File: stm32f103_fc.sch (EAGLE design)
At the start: 49 parts, among them IC1 STM32F10XCXT6, IC2 LD1117AS33TR, U2 9DoF IMU, Y1 8MHz, Y2 32.768MHz

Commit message: version 2.0
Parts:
- removed C11, C13, C14, C7: 0.1uF, SparkFun-Capacitors:0.1UF-0402-16V-10%
- removed S1: SPST-SMD-5.2, SparkFun-Switches:MOMENTARY-SWITCH-SPST-SMD-5.2-REDUNDANT
- removed U2: 9DoF IMU, SparkFun-Sensors:MPU-9250
- added BUZZER: CMT-1285C-035, SparkFun-Electromechanical:BUZZER-PTH
- added C15, C22: 0.1uF, SparkFun-Capacitors:0.1UF-0402-16V-10%
- added C19: 2.2nF, SparkFun-Capacitors:2.2NF/2200PF-0603-50V-10%
- added C23: 10nF, SparkFun-Capacitors:10NF-0603-50V-10%
- added IMU: MPU-6050, MPU-6050:MPU-6050
- added SWITCH: MOMENTARY-SWITCH-SPST-SMD-4.5MM-轻触开关, SparkFun-Switches:MOMENTARY-SWITCH-SPST-SMD-4.5MM
- C18: device SparkFun-Capacitors:0.1UF-0603-25V-(+80/-20%) -> SparkFun-Capacitors:0.1UF-0402-16V-10%
- C5: value 10nF -> 0.1uF; device SparkFun-Capacitors:10NF-0603-50V-10% -> SparkFun-Capacitors:0.1UF-0402-16V-10%
- C6: device SparkFun-Capacitors:0.1UF-0402-16V-10% -> SparkFun-Capacitors:0.1UF-0603-25V-(+80/-20%)
- HEADER: value (none) -> 2.54mm 2PX3P header
- IC1: value STM32F10XCXT6 -> STM32F103C8T6
- LED1, LED2: value GREEN -> BL-HGE36G-AV-TRB
- MICRO-USB: value (none) -> Micro-USB-5P-无柱-SMD
- N-CHANNEL-MOSFET, N-CHANNEL-MOSFET-2: value (none) -> 2N7002KT1G
- POWER_INPUT: value (none) -> KF350-2P-terminal-block-接线端子
- PY1, PY2: value 1X2-3.5MM -> 1X2-3.5MM KF350 terminal block
- R10, R13: value 22 -> 22omh
- R11, R9: value 680 -> 680omh
- R4, R5: value 470 -> 470omh
- SERVO_X, SERVO_Y: value (none) -> 2.54mm 3P header
- SWD: value (none) -> 2.54mm 4P header
- renumbered D1 to LED1, D2 to LED2, J3 to MICRO-USB, Q1 to N-CHANNEL-MOSFET, Q2 to N-CHANNEL-MOSFET-2
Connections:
- removed net N$11: C6.2, U2.REGOUT
- removed net N$28: IC1POWER.VSS_2
- removed net N$30: IC1POWER.VDD_2
- removed net N$31: IC1POWER.VDD_1
- removed net VBAT: IC1AN_POWER.VBAT
- new net N$16: C22.2, IMU.REGOUT
- new net N$4: C19.1, IMU.CPOUT
- net 9V: now also C6.2; no longer MICRO-USB.VBUS
- net GND: now also BUZZER.2, C15.1, C18.1, C19.2, C22.1, C23.1, C4.2, C5.1, C8.2, IC1POWER.VSS_2, IMU.CLKIN, IMU.FSYNC, IMU.GND, SWITCH.1; no longer C11.2, C13.2, C14.2, C18.2, C5.2, C6.1, C7.2, S1.1, U2.FSYNC, U2.GND
- net N$10: now also C6.1, MICRO-USB.VBUS; no longer C4.2, C8.2
- net PA12: no longer U2.INT
- net PB0: now also IMU.INT
- net PB1: now also BUZZER.1
- net PB8: now also IMU.SDA; no longer U2.SDA/SDI
- net PB9: now also IMU.SCL; no longer U2.SCL/SCLK
- net RESET: now also SWITCH.2; no longer S1.2
- net VCC3V3: now also C15.2, C18.2, C23.2, C5.2, IC1AN_POWER.VBAT, IC1POWER.VDD_1, IC1POWER.VDD_2, IMU.VDD, IMU.VLOGIC; no longer C11.1, C13.1, C14.1, C18.1, C5.1, C7.1, U2.!CS, U2.VDD, U2.VDDIO
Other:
- note removed: "checked"
- moved on the sheet: C18, C5, C6

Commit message: version 1.0.1 done fix transistor
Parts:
- removed N-CHANNEL-MOSFET: 2N7002KT1G, adafruit:MOSFET-NREFLOW
- removed R12: 1omh, SparkFun-Resistors:1OHM-0603-1/10W-1%
- added MOSFET-1: 2N7002KT1G, adafruit:MOSFET-NREFLOW
- added R14: 470omh, SparkFun-Resistors:470OHM-0603-1/10W-1%
- R4: value 470omh -> 1omh; device SparkFun-Resistors:470OHM-0603-1/10W-1% -> SparkFun-Resistors:1OHM-0603-1/10W-1%
- renumbered N-CHANNEL-MOSFET-2 to MOSFET-2
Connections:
- removed net N$15: N-CHANNEL-MOSFET.D, R12.1
- new net N$11: PY1.2, R4.2
- net GND: now also MOSFET-1.D, MOSFET-2.D, R14.2, R5.2; no longer MOSFET-2.S, N-CHANNEL-MOSFET.S, R4.1, R5.1
- net N$13: now also MOSFET-2.S; no longer MOSFET-2.D
- net N$14: now also MOSFET-1.S, R4.1; no longer PY1.2, R12.2
- net PB6: now also R14.1; no longer R5.2
- net PB7: now also MOSFET-1.G, R5.1; no longer N-CHANNEL-MOSFET.G, R4.2
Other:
- moved on the sheet: R15, R4, R5

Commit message: added new switch
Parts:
- SWITCH: device SparkFun-Switches:MOMENTARY-SWITCH-SPST-SMD-4.5MM -> SparkFun-Switches:MOMENTARY-SWITCH-SPST-SMD-6.0X3.5MM
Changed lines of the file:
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@@
 <?xml version="1.0" encoding="utf-8"?>
 <!DOCTYPE eagle SYSTEM "eagle.dtd">
-<eagle version="9.3.1">
+<eagle version="9.3.0">
 <drawing>
 <settings>
@@
 <grid distance="0.1" unitdist="inch" unit="inch" style="lines" multiple="1" display="no" altdistance="0.01" altunitdist="inch" altunit="inch"/>
 <layers>
-<layer number="1" name="Top" color="4" fill="1" visible="no" active="no"/>
-<layer number="16" name="Bottom" color="1" fill="1" visible="no" active="no"/>
-<layer number="17" name="Pads" color="2" fill="1" visible="no" active="no"/>
-<layer number="18" name="Vias" color="2" fill="1" visible="no" active="no"/>
-<layer number="19" name="Unrouted" color="6" fill="1" visible="no" active="no"/>
-<layer number="20" name="Dimension" color="24" fill="1" visible="no" active="no"/>
-<layer number="21" name="tPlace" color="7" fill="1" visible="no" active="no"/>
-<layer number="22" name="bPlace" color="7" fill="1" visible="no" active="no"/>
-<layer number="23" name="tOrigins" color="15" fill="1" visible="no" active="no"/>
-<layer number="24" name="bOrigins" color="15" fill="1" visible="no" active="no"/>
-<layer number="25" name="tNames" color="7" fill="1" visible="no" active="no"/>
-<layer number="26" name="bNames" color="7" fill="1" visible="no" active="no"/>
-<layer number="27" name="tValues" color="7" fill="1" visible="no" active="no"/>
-<layer number="28" name="bValues" color="7" fill="1" visible="no" active="no"/>
+<layer number="1" name="Top" color="4" fill="1" visible="yes" active="no"/>
+<layer number="16" name="Bottom" color="1" fill="1" visible="yes" active="no"/>
+<layer number="17" name="Pads" color="2" fill="1" visible="yes" active="no"/>
+<layer number="18" name="Vias" color="2" fill="1" visible="yes" active="no"/>
+<layer number="19" name="Unrouted" color="6" fill="1" visible="yes" active="no"/>
+<layer number="20" name="Dimension" color="24" fill="1" visible="yes" active="no"/>
+<layer number="21" name="tPlace" color="7" fill="1" visible="yes" active="no"/>
+<layer number="22" name="bPlace" color="7" fill="1" visible="yes" active="no"/>
+<layer number="23" name="tOrigins" color="15" fill="1" visible="yes" active="no"/>
+<layer number="24" name="bOrigins" color="15" fill="1" visible="yes" active="no"/>
+<layer number="25" name="tNames" color="7" fill="1" visible="yes" active="no"/>
+<layer number="26" name="bNames" color="7" fill="1" visible="yes" active="no"/>
+<layer number="27" name="tValues" color="7" fill="1" visible="yes" active="no"/>
+<layer number="28" name="bValues" color="7" fill="1" visible="yes" active="no"/>
 <layer number="29" name="tStop" color="7" fill="3" visible="no" active="no"/>
 <layer number="30" name="bStop" color="7" fill="6" visible="no" active="no"/>
@@
 <layer number="35" name="tGlue" color="7" fill="4" visible="no" active="no"/>
 <layer number="36" name="bGlue" color="7" fill="5" visible="no" active="no"/>
-<layer number="37" name="tTest" color="7" fill="1" visible="no" active="no"/>
-<layer number="38" name="bTest" color="7" fill="1" visible="no" active="no"/>
+<layer number="37" name="tTest" color="7" fill="1" visible="yes" active="no"/>
+<layer number="38" name="bTest" color="7" fill="1" visible="yes" active="no"/>
 <layer number="39" name="tKeepout" color="4" fill="11" visible="no" active="no"/>
 <layer number="40" name="bKeepout" color="1" fill="11" visible="no" active="no"/>
@@
 <layer number="44" name="Drills" color="7" fill="1" visible="no" active="no"/>
 <layer number="45" name="Holes" color="7" fill="1" visible="no" active="no"/>
-<layer number="46" name="Milling" color="3" fill="1" visible="no" active="no"/>
-<layer number="47" name="Measures" color="7" fill="1" visible="no" active="no"/>
-<layer number="48" name="Document" color="7" fill="1" visible="no" active="no"/>
-<layer number="49" name="Reference" color="7" fill="1" visible="no" active="no"/>
-<layer number="50" name="dxf" color="7" fill="1" visible="no" active="no"/>
-<layer number="51" name="tDocu" color="7" fill="1" visible="no" active="no"/>
-<layer number="52" name="bDocu" color="7" fill="1" visible="no" active="no"/>
-<layer number="53" name="tGND_GNDA" color="7" fill="9" visible="no" active="no"/>
-<layer number="54" name="bGND_GNDA" color="1" fill="9" visible="no" active="no"/>
-<layer number="56" name="wert" color="7" fill="1" visible="no" active="no"/>
-<layer number="57" name="tCAD" color="7" fill="1" visible="no" active="no"/>
-<layer number="59" name="tCarbon" color="7" fill="1" visible="no" active="no"/>
-<layer number="60" name="bCarbon" color="7" fill="1" visible="no" active="no"/>
+<layer number="46" name="Milling" color="3" fill="1" visible="yes" active="no"/>
+<layer number="47" name="Measures" color="7" fill="1" visible="yes" active="no"/>
+<layer number="48" name="Document" color="7" fill="1" visible="yes" active="no"/>
+<layer number="49" name="Reference" color="7" fill="1" visible="yes" active="no"/>
+<layer number="50" name="dxf" color="7" fill="1" visible="yes" active="no"/>
+<layer number="51" name="tDocu" color="7" fill="1" visible="yes" active="no"/>
+<layer number="52" name="bDocu" color="7" fill="1" visible="yes" active="no"/>
+<layer number="53" name="tGND_GNDA" color="7" fill="9" visible="yes" active="no"/>
+<layer number="54" name="bGND_GNDA" color="1" fill="9" visible="yes" active="no"/>
+<layer number="56" name="wert" color="7" fill="1" visible="yes" active="no"/>
+<layer number="57" name="tCAD" color="7" fill="1" visible="yes" active="no"/>
+<layer number="59" name="tCarbon" color="7" fill="1" visible="yes" active="no"/>
+<layer number="60" name="bCarbon" color="7" fill="1" visible="yes" active="no"/>
 <layer number="88" name="SimResults" color="9" fill="1" visible="yes" active="yes"/>
 <layer number="89" name="SimProbes" color="9" fill="1" visible="yes" active="yes"/>
@@
 <part name="C18" library="SparkFun-Capacitors" deviceset="0.1UF" device="-0402-16V-10%" value="0.1uF"/>
 <part name="GND12" library="SparkFun-PowerSymbols" library_urn="urn:adsk.eagle:library:530" deviceset="GND" device=""/>
-<part name="SWITCH" library="SparkFun-Switches" library_urn="urn:adsk.eagle:library:535" deviceset="MOMENTARY-SWITCH-SPST" device="-SMD-4.5MM" package3d_urn="urn:adsk.eagle:package:40162/1" value="MOMENTARY-SWITCH-SPST-SMD-4.5MM-轻触开关"/>
+<part name="SWITCH" library="SparkFun-Switches" library_urn="urn:adsk.eagle:library:535" deviceset="MOMENTARY-SWITCH-SPST" device="-SMD-6.0X3.5MM" package3d_urn="urn:adsk.eagle:package:40165/1" value="MOMENTARY-SWITCH-SPST-SMD-4.5MM-轻触开关"/>
 <part name="R14" library="SparkFun-Resistors" library_urn="urn:adsk.eagle:library:532" deviceset="470OHM" device="-0603-1/10W-1%" package3d_urn="urn:adsk.eagle:package:39650/1" value="470omh"/>
 <part name="GND13" library="SparkFun-PowerSymbols" library_urn="urn:adsk.eagle:library:530" deviceset="GND" device=""/>

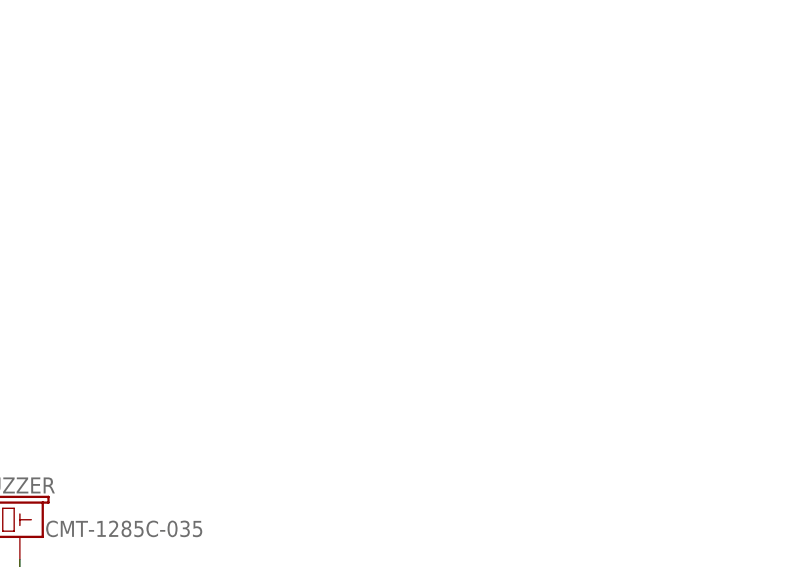
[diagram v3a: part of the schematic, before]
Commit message: added serial port
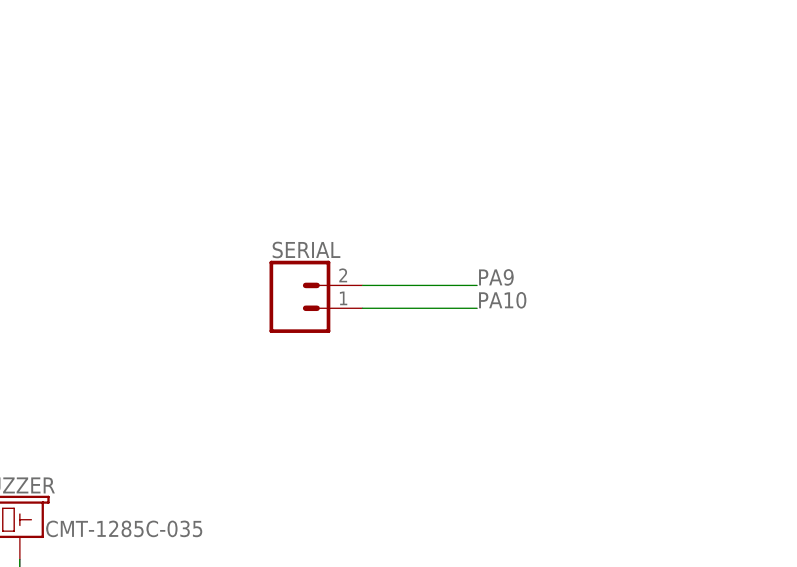
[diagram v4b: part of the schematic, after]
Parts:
- added SERIAL: (no value), SparkFun-Connectors:CONN_02
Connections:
- net PA10: now also SERIAL.1
- net PA9: now also SERIAL.2
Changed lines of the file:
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@@
 <grid distance="0.1" unitdist="inch" unit="inch" style="lines" multiple="1" display="no" altdistance="0.01" altunitdist="inch" altunit="inch"/>
 <layers>
-<layer number="1" name="Top" color="4" fill="1" visible="yes" active="no"/>
-<layer number="16" name="Bottom" color="1" fill="1" visible="yes" active="no"/>
-<layer number="17" name="Pads" color="2" fill="1" visible="yes" active="no"/>
-<layer number="18" name="Vias" color="2" fill="1" visible="yes" active="no"/>
-<layer number="19" name="Unrouted" color="6" fill="1" visible="yes" active="no"/>
-<layer number="20" name="Dimension" color="24" fill="1" visible="yes" active="no"/>
-<layer number="21" name="tPlace" color="7" fill="1" visible="yes" active="no"/>
-<layer number="22" name="bPlace" color="7" fill="1" visible="yes" active="no"/>
-<layer number="23" name="tOrigins" color="15" fill="1" visible="yes" active="no"/>
-<layer number="24" name="bOrigins" color="15" fill="1" visible="yes" active="no"/>
-<layer number="25" name="tNames" color="7" fill="1" visible="yes" active="no"/>
-<layer number="26" name="bNames" color="7" fill="1" visible="yes" active="no"/>
-<layer number="27" name="tValues" color="7" fill="1" visible="yes" active="no"/>
-<layer number="28" name="bValues" color="7" fill="1" visible="yes" active="no"/>
+<layer number="1" name="Top" color="4" fill="1" visible="no" active="no"/>
+<layer number="2" name="Route2" color="16" fill="1" visible="no" active="no"/>
+<layer number="3" name="Route3" color="17" fill="1" visible="no" active="no"/>
+<layer number="4" name="Route4" color="18" fill="1" visible="no" active="no"/>
+<layer number="5" name="Route5" color="19" fill="1" visible="no" active="no"/>
+<layer number="6" name="Route6" color="25" fill="1" visible="no" active="no"/>
+<layer number="7" name="Route7" color="26" fill="1" visible="no" active="no"/>
+<layer number="8" name="Route8" color="27" fill="1" visible="no" active="no"/>
+<layer number="9" name="Route9" color="28" fill="1" visible="no" active="no"/>
+<layer number="10" name="Route10" color="29" fill="1" visible="no" active="no"/>
+<layer number="11" name="Route11" color="30" fill="1" visible="no" active="no"/>
+<layer number="12" name="Route12" color="20" fill="1" visible="no" active="no"/>
+<layer number="13" name="Route13" color="21" fill="1" visible="no" active="no"/>
+<layer number="14" name="Route14" color="22" fill="1" visible="no" active="no"/>
+<layer number="15" name="Route15" color="23" fill="1" visible="no" active="no"/>
+<layer number="16" name="Bottom" color="1" fill="1" visible="no" active="no"/>
+<layer number="17" name="Pads" color="2" fill="1" visible="no" active="no"/>
+<layer number="18" name="Vias" color="2" fill="1" visible="no" active="no"/>
+<layer number="19" name="Unrouted" color="6" fill="1" visible="no" active="no"/>
+<layer number="20" name="Dimension" color="24" fill="1" visible="no" active="no"/>
+<layer number="21" name="tPlace" color="7" fill="1" visible="no" active="no"/>
+<layer number="22" name="bPlace" color="7" fill="1" visible="no" active="no"/>
+<layer number="23" name="tOrigins" color="15" fill="1" visible="no" active="no"/>
+<layer number="24" name="bOrigins" color="15" fill="1" visible="no" active="no"/>
+<layer number="25" name="tNames" color="7" fill="1" visible="no" active="no"/>
+<layer number="26" name="bNames" color="7" fill="1" visible="no" active="no"/>
+<layer number="27" name="tValues" color="7" fill="1" visible="no" active="no"/>
+<layer number="28" name="bValues" color="7" fill="1" visible="no" active="no"/>
 <layer number="29" name="tStop" color="7" fill="3" visible="no" active="no"/>
 <layer number="30" name="bStop" color="7" fill="6" visible="no" active="no"/>
@@
 <layer number="35" name="tGlue" color="7" fill="4" visible="no" active="no"/>
 <layer number="36" name="bGlue" color="7" fill="5" visible="no" active="no"/>
-<layer number="37" name="tTest" color="7" fill="1" visible="yes" active="no"/>
-<layer number="38" name="bTest" color="7" fill="1" visible="yes" active="no"/>
+<layer number="37" name="tTest" color="7" fill="1" visible="no" active="no"/>
+<layer number="38" name="bTest" color="7" fill="1" visible="no" active="no"/>
 <layer number="39" name="tKeepout" color="4" fill="11" visible="no" active="no"/>
 <layer number="40" name="bKeepout" color="1" fill="11" visible="no" active="no"/>
@@
 <layer number="44" name="Drills" color="7" fill="1" visible="no" active="no"/>
 <layer number="45" name="Holes" color="7" fill="1" visible="no" active="no"/>
-<layer number="46" name="Milling" color="3" fill="1" visible="yes" active="no"/>
-<layer number="47" name="Measures" color="7" fill="1" visible="yes" active="no"/>
-<layer number="48" name="Document" color="7" fill="1" visible="yes" active="no"/>
-<layer number="49" name="Reference" color="7" fill="1" visible="yes" active="no"/>
-<layer number="50" name="dxf" color="7" fill="1" visible="yes" active="no"/>
-<layer number="51" name="tDocu" color="7" fill="1" visible="yes" active="no"/>
-<layer number="52" name="bDocu" color="7" fill="1" visible="yes" active="no"/>
-<layer number="53" name="tGND_GNDA" color="7" fill="9" visible="yes" active="no"/>
-<layer number="54" name="bGND_GNDA" color="1" fill="9" visible="yes" active="no"/>
-<layer number="56" name="wert" color="7" fill="1" visible="yes" active="no"/>
-<layer number="57" name="tCAD" color="7" fill="1" visible="yes" active="no"/>
-<layer number="59" name="tCarbon" color="7" fill="1" visible="yes" active="no"/>
-<layer number="60" name="bCarbon" color="7" fill="1" visible="yes" active="no"/>
+<layer number="46" name="Milling" color="3" fill="1" visible="no" active="no"/>
+<layer number="47" name="Measures" color="7" fill="1" visible="no" active="no"/>
+<layer number="48" name="Document" color="7" fill="1" visible="no" active="no"/>
+<layer number="49" name="Reference" color="7" fill="1" visible="no" active="no"/>
+<layer number="50" name="dxf" color="7" fill="1" visible="no" active="no"/>
+<layer number="51" name="tDocu" color="7" fill="1" visible="no" active="no"/>
+<layer number="52" name="bDocu" color="7" fill="1" visible="no" active="no"/>
+<layer number="53" name="tGND_GNDA" color="7" fill="9" visible="no" active="no"/>
+<layer number="54" name="bGND_GNDA" color="1" fill="9" visible="no" active="no"/>
+<layer number="56" name="wert" color="7" fill="1" visible="no" active="no"/>
+<layer number="57" name="tCAD" color="7" fill="1" visible="no" active="no"/>
+<layer number="59" name="tCarbon" color="7" fill="1" visible="no" active="no"/>
+<layer number="60" name="bCarbon" color="7" fill="1" visible="no" active="no"/>
 <layer number="88" name="SimResults" color="9" fill="1" visible="yes" active="yes"/>
 <layer number="89" name="SimProbes" color="9" fill="1" visible="yes" active="yes"/>
@@
 <part name="R5" library="SparkFun-Resistors" library_urn="urn:adsk.eagle:library:532" deviceset="470OHM" device="-0603-1/10W-1%" package3d_urn="urn:adsk.eagle:package:39650/1" value="470omh"/>
 <part name="GND14" library="SparkFun-PowerSymbols" library_urn="urn:adsk.eagle:library:530" deviceset="GND" device=""/>
+<part name="SERIAL" library="SparkFun-Connectors" library_urn="urn:adsk.eagle:library:513" deviceset="CONN_02" device="" package3d_urn="urn:adsk.eagle:package:38039/1"/>
 </parts>
 <sheets>
@@
 <instance part="GND14" gate="1" x="-50.8" y="200.66" smashed="yes" rot="R180">
 <attribute name="VALUE" x="-50.8" y="200.914" size="1.778" layer="96" rot="R180" align="top-center"/>
+</instance>
+<instance part="SERIAL" gate="G$1" x="149.86" y="147.32" smashed="yes">
+<attribute name="VALUE" x="147.32" y="142.494" size="1.778" layer="96" font="vector"/>
+<attribute name="NAME" x="147.32" y="152.908" size="1.778" layer="95" font="vector"/>
 </instance>
 </instances>
@@
 <label x="86.36" y="71.12" size="1.778" layer="95"/>
 </segment>
+<segment>
+<pinref part="SERIAL" gate="G$1" pin="1"/>
+<wire x1="157.48" y1="147.32" x2="170.18" y2="147.32" width="0.1524" layer="91"/>
+<label x="170.18" y="147.32" size="1.778" layer="95"/>
+</segment>
 </net>
 <net name="PA9" class="0">
@@
 <label x="86.36" y="68.58" size="1.778" layer="95"/>
 </segment>
-</net>
+<segment>
+<pinref part="SERIAL" gate="G$1" pin="2"/>
+<wire x1="157.48" y1="149.86" x2="170.18" y2="149.86" width="0.1524" layer="91"/>
+<label x="170.18" y="149.86" size="1.778" layer="95"/>
+</segment>
+</net>
